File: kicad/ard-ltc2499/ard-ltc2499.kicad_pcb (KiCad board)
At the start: 2 copper layers, 53.3 x 68.6 mm, 55 parts, among them J1 Screw_Terminal_01x02, J2 Screw_Terminal_01x08, J3 Screw_Terminal_01x08, P1 Power, P2 Analog, P3 Digital, P4 Digital, P5 CONN_01X01, P6 CONN_01X01, P7 CONN_01X01, P8 CONN_01X01, Q1 BSS138, Q2 BSS138, SW1 SW_DIP_x08, SW2 JS202011SCQN, U1 LTC2499CUHF-PBF, U2 LT6654xxS6, U3 AP7381-50Y, U4 24AA025E64

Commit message: Adjusted text
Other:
- board text added: "+"
- board text added: "Arduino 5V"
- board text added: "Onboard 5V Reg"
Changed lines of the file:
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@@
   )
   (gr_line (start 150.749 116.586) (end 150.749 102.362) (layer "F.SilkS") (width 0.15))
+  (gr_line (start 134.0485 92.964) (end 137.9855 92.964) (layer "F.SilkS") (width 0.15))
   (gr_line (start 150.749 102.362) (end 154.051 102.362) (layer "F.SilkS") (width 0.15))
   (gr_poly
@@
   (gr_line (start 152.146 117.602) (end 152.146 121.666) (layer "F.SilkS") (width 0.15))
   (gr_line (start 150.749 116.586) (end 154.051 116.586) (layer "F.SilkS") (width 0.15))
+  (gr_line (start 128.9685 92.964) (end 132.9055 92.964) (layer "F.SilkS") (width 0.15))
   (gr_line (start 120.269 78.994) (end 114.427 78.994) (layer "Dwgs.User") (width 0.15))
   (gr_line (start 120.269 74.93) (end 120.269 78.994) (layer "Dwgs.User") (width 0.15))
@@
     (effects (font (size 0.889 0.7366) (thickness 0.1524)))
   )
+  (gr_text "Onboard\n5V Reg" (at 136.017 91.186) (layer "F.SilkS")
+    (effects (font (size 0.889 0.7366) (thickness 0.1524)))
+  )
   (gr_text "PWR" (at 137.16 119.38) (layer "F.SilkS")
     (effects (font (size 1.524 1.524) (thickness 0.3048)))
@@
     (effects (font (size 0.889 0.7366) (thickness 0.1524)))
   )
+  (gr_text "*" (at 161.671 75.692) (layer "F.SilkS")
+    (effects (font (size 1 1) (thickness 0.15)))
+  )
   (gr_text "0   1   2   3   4   5   6   7" (at 130.81 65.278 180) (layer "F.SilkS")
     (effects (font (size 1.016 0.7874) (thickness 0.1524)))
@@
     (effects (font (size 1.016 1.016) (thickness 0.1524)) (justify right))
   )
-  (gr_text "ARD-LTC2499 v2.0\nIowa Scaled Engineering\nhttp://www.iascaled.com\nCC BY-SA ©2024" (at 121.158 85.598) (layer "F.SilkS")
+  (gr_text "ARD-LTC2499 v2.0\nIowa Scaled Engineering\nhttp://www.iascaled.com\nCC BY-SA ©2024" (at 121.158 85.09) (layer "F.SilkS")
     (effects (font (size 1.016 1.016) (thickness 0.1524)) (justify left))
   )
@@
     (effects (font (size 0.7874 0.762) (thickness 0.1524)) (justify left))
   )
+  (gr_text "+" (at 131.191 121.031) (layer "F.SilkS")
+    (effects (font (size 1 1) (thickness 0.15)))
+  )
   (gr_text "CA2\nL   H" (at 152.4 104.394 90) (layer "F.SilkS")
     (effects (font (size 0.889 0.7366) (thickness 0.1524)))
@@
     (effects (font (size 1.016 0.7874) (thickness 0.1524)))
   )
+  (gr_text "Arduino\n5V" (at 130.937 91.186) (layer "F.SilkS")
+    (effects (font (size 0.889 0.7366) (thickness 0.1524)))
+  )
   (gr_text "10  11  12  13  14  15" (at 143.764 131.572) (layer "F.SilkS")
     (effects (font (size 1.016 0.7366) (thickness 0.1524)))
@@
     (effects (font (size 1.016 0.7874) (thickness 0.1524)) (justify left))
   )
-  (gr_text "*" (at 149.479 106.934) (layer "F.SilkS")
+  (gr_text "*" (at 149.479 107.061) (layer "F.SilkS")
     (effects (font (size 1 1) (thickness 0.15)))
   )

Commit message: Minor tweaks
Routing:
- net GND: track 112.0 -> 99.5 mm
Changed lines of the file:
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@@
     (property "Voltage" "16V")
     (attr smd)
-    (fp_text reference "C3" (at -0.254 -1.778) (layer "F.SilkS")
+    (fp_text reference "C3" (at 0 -1.778) (layer "F.SilkS")
       (effects (font (size 1 1) (thickness 0.15)))
     )
@@
   (segment (start 143.768 89.6226) (end 143.768 73.529) (width 0.25) (layer "F.Cu") (net 4))
   (segment (start 146.768 89.6226) (end 146.768 90.279) (width 0.254) (layer "F.Cu") (net 4))
-  (segment (start 166.116 123.317) (end 153.289 123.317) (width 0.381) (layer "F.Cu") (net 4))
   (segment (start 166.878 110.744) (end 167.005 110.871) (width 0.381) (layer "F.Cu") (net 4))
   (segment (start 133.5255 119.38) (end 133.5255 120.8555) (width 0.25) (layer "F.Cu") (net 4))
@@
   (segment (start 132.588 109.855) (end 132.588 108.331) (width 0.762) (layer "F.Cu") (net 4))
   (segment (start 146.768 94.5274) (end 148.6294 94.5274) (width 0.25) (layer "F.Cu") (net 4))
-  (segment (start 167.005 120.904) (end 167.005 122.428) (width 0.381) (layer "F.Cu") (net 4))
   (segment (start 147.470401 93.075001) (end 145.018001 93.075001) (width 0.25) (layer "F.Cu") (net 4))
   (segment (start 145.018001 93.075001) (end 144.018 92.075) (width 0.25) (layer "F.Cu") (net 4))
   (segment (start 144.517999 92.574999) (end 144.018 92.075) (width 0.25) (layer "F.Cu") (net 4))
-  (segment (start 167.005 122.428) (end 166.116 123.317) (width 0.381) (layer "F.Cu") (net 4))
   (segment (start 160.02 76.835) (end 160.02 75.311) (width 0.254) (layer "F.Cu") (net 4))
   (segment (start 167.005 110.871) (end 167.005 115.824) (width 0.381) (layer "F.Cu") (net 4))
@@
   (segment (start 167.005 115.824) (end 167.005 118.364) (width 0.381) (layer "F.Cu") (net 4))
   (segment (start 164.452 105.664) (end 166.37 105.664) (width 0.381) (layer "F.Cu") (net 4))
+  (segment (start 167.005 123.444) (end 167.005 120.904) (width 0.381) (layer "F.Cu") (net 4))
   (segment (start 166.37 105.664) (end 167.005 106.299) (width 0.381) (layer "F.Cu") (net 4))
   (segment (start 147.470401 92.574999) (end 148.708999 92.574999) (width 0.25) (layer "F.Cu") (net 4))
   (segment (start 162.179 76.962) (end 163.5155 76.962) (width 0.381) (layer "F.Cu") (net 4))
+  (segment (start 166.624 123.825) (end 167.005 123.444) (width 0.381) (layer "F.Cu") (net 4))
   (segment (start 145.268 89.6226) (end 145.268 90.825) (width 0.25) (layer "F.Cu") (net 4))
   (segment (start 147.470401 93.075001) (end 148.701001 93.075001) (width 0.25) (layer "F.Cu") (net 4))
@@
   (segment (start 144.82 72.477) (end 144.82 70.104) (width 0.25) (layer "F.Cu") (net 4))
   (segment (start 163.5155 76.962) (end 163.576 77.0225) (width 0.381) (layer "F.Cu") (net 4))
-  (via (at 153.289 123.317) (size 0.6) (drill 0.4) (layers "F.Cu" "B.Cu") (net 4))
+  (via (at 166.624 123.825) (size 0.6) (drill 0.4) (layers "F.Cu" "B.Cu") (net 4))
   (via (at 150.114 103.251) (size 0.6) (drill 0.4) (layers "F.Cu" "B.Cu") (free) (net 4))
   (via (at 160.02 75.311) (size 0.6) (drill 0.4) (layers "F.Cu" "B.Cu") (net 4))
@@
     (polygon
       (pts
-        (xy 153.796998 72.136)
-        (xy 164.465 72.136)
-        (xy 164.465 86.106)
-        (xy 153.796998 86.106)
-        (xy 153.796998 123.824376)
-        (xy 120.269 123.825)
+        (xy 167.386 72.136)
+        (xy 167.38601 124.713376)
+        (xy 120.269012 124.714)
         (xy 120.142 72.136)
-        (xy 153.796998 72.135376)
       )
     )

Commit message: Minor updates to text
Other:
- board text added: "A0 A1 L L"
- board text removed: "AD0 AD1"
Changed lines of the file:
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@@
     )
     (pad_to_mask_clearance 0)
-    (aux_axis_origin 110.998 126.365)
+    (aux_axis_origin 119.634 132.715)
     (pcbplotparams
       (layerselection 0x0000030_80000001)
@@
   )
   (gr_line (start 150.749 116.586) (end 150.749 102.362) (layer "F.SilkS") (width 0.15))
+  (gr_line (start 150.749 117.348) (end 154.051 117.348) (layer "F.SilkS") (width 0.15))
   (gr_line (start 134.0485 92.964) (end 137.9855 92.964) (layer "F.SilkS") (width 0.15))
   (gr_line (start 150.749 102.362) (end 154.051 102.362) (layer "F.SilkS") (width 0.15))
@@
       (xy 148.107136 78.517728)
     ) (layer "F.SilkS") (width 0) (fill solid))
+  (gr_line (start 150.749 121.92) (end 154.051 121.92) (layer "F.SilkS") (width 0.15))
   (gr_poly
     (pts
@@
       (xy 144.291095 76.196139)
     ) (layer "F.SilkS") (width 0) (fill solid))
-  (gr_line (start 152.146 117.602) (end 152.146 121.666) (layer "F.SilkS") (width 0.15))
+  (gr_line (start 150.749 117.348) (end 150.749 121.92) (layer "F.SilkS") (width 0.15))
   (gr_line (start 150.749 116.586) (end 154.051 116.586) (layer "F.SilkS") (width 0.15))
   (gr_line (start 128.9685 92.964) (end 132.9055 92.964) (layer "F.SilkS") (width 0.15))
@@
   (gr_line (start 172.974 128.651) (end 172.974 64.135) (layer "Edge.Cuts") (width 0.15))
   (gr_line (start 160.02 130.175) (end 171.45 130.175) (layer "Edge.Cuts") (width 0.15))
-  (gr_text "EEP ADR" (at 151.257 119.634 90) (layer "F.SilkS")
+  (gr_text "EEP ADR" (at 149.86 119.634 90) (layer "F.SilkS")
     (effects (font (size 0.889 0.7366) (thickness 0.1524)))
   )
@@
     (effects (font (size 0.7874 0.762) (thickness 0.1524)) (justify left))
   )
-  (gr_text "LTC2499 ADR" (at 149.987 116.713 90) (layer "F.SilkS")
+  (gr_text "LTC2499 ADR" (at 149.86 116.713 90) (layer "F.SilkS")
     (effects (font (size 0.889 0.7366) (thickness 0.1524)) (justify left))
   )
@@
     (effects (font (size 0.889 0.7366) (thickness 0.1524)))
   )
-  (gr_text "\nAD0 AD1" (at 152.4 119.634 90) (layer "F.SilkS")
+  (gr_text "A0  A1\nL   L" (at 152.4 119.634 90) (layer "F.SilkS")
     (effects (font (size 0.889 0.7366) (thickness 0.1524)))
   )
@@
     (effects (font (size 1.016 0.7366) (thickness 0.1524)))
   )
-  (gr_text "4.096V REF   COM" (at 154.686 65.278 180) (layer "F.SilkS")
+  (gr_text "4.096V REF  COM" (at 154.178 65.278 180) (layer "F.SilkS")
     (effects (font (size 1.016 0.7874) (thickness 0.1524)) (justify left))
   )

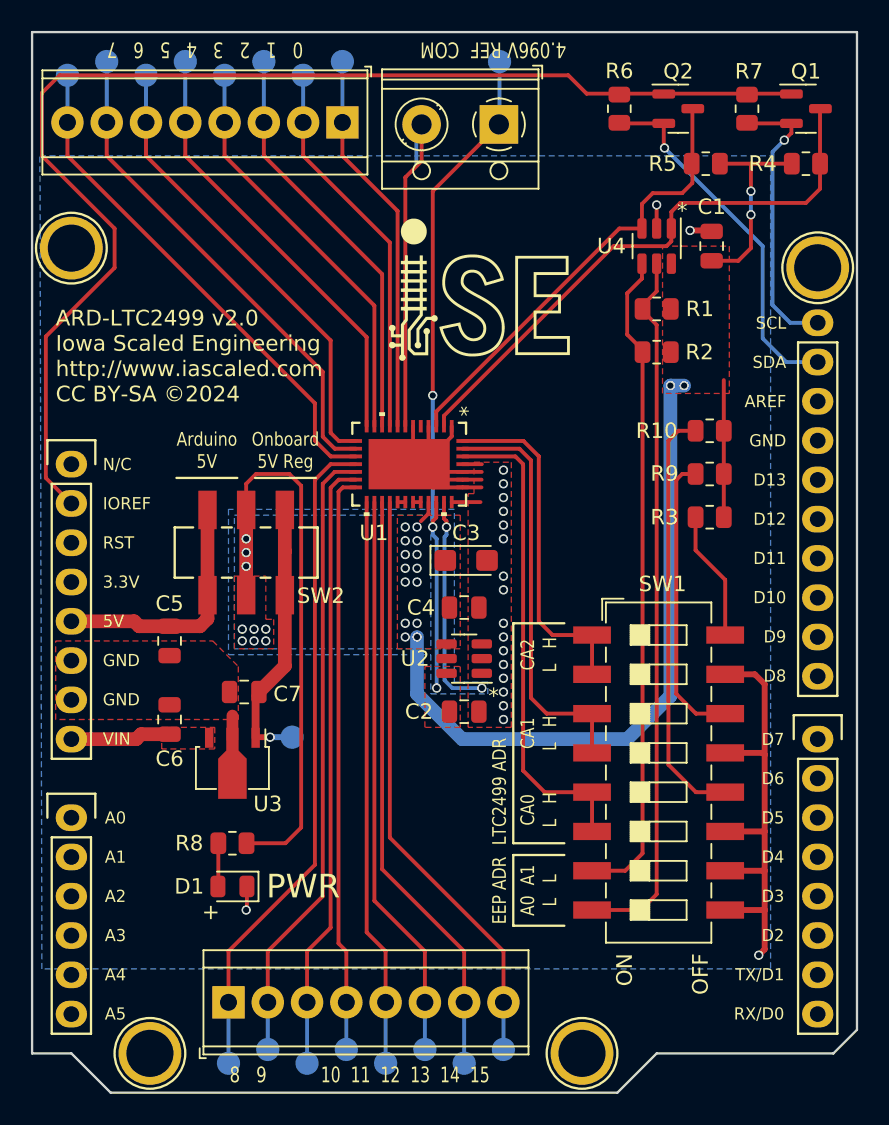
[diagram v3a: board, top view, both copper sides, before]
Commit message: Minor adjustments to metal traces
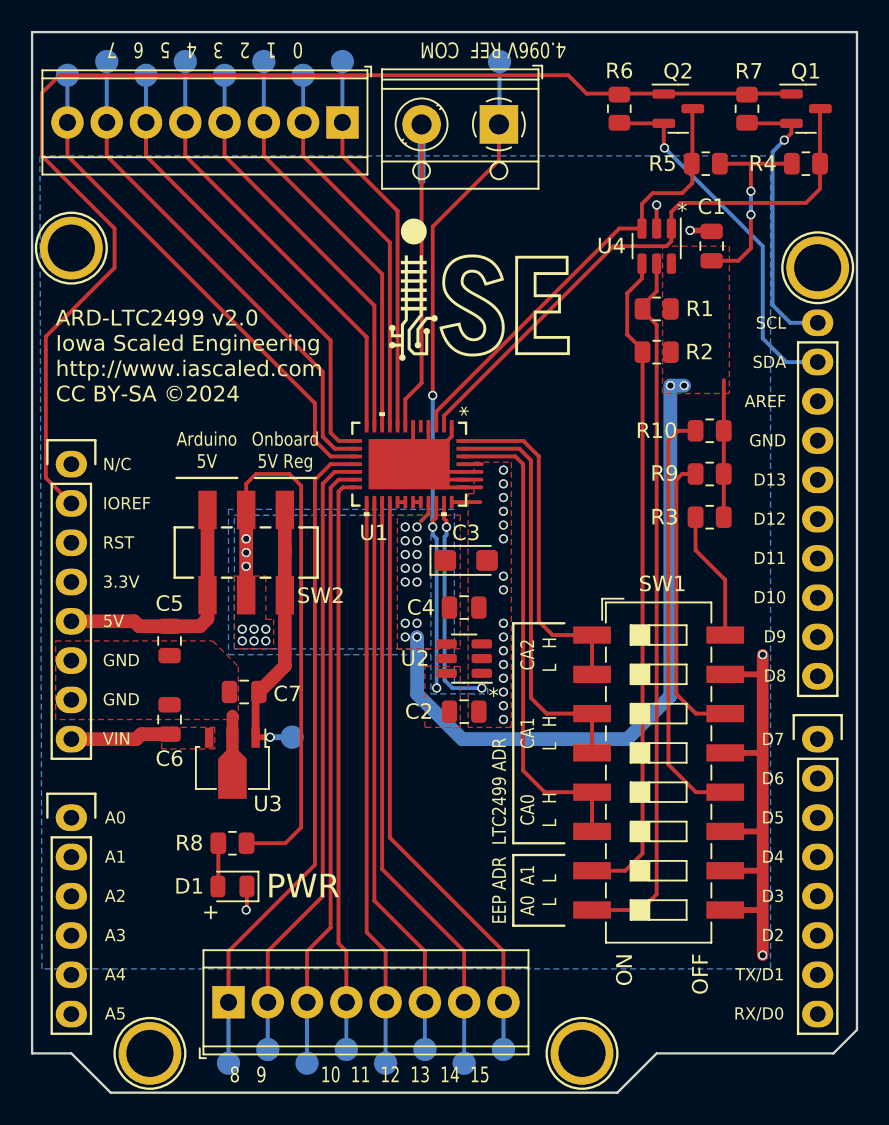
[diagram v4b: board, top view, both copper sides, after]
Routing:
- net GND: track 99.5 -> 102.1 mm, vias 22 -> 23
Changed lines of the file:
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@@
   (segment (start 130.977 95.0341) (end 130.977 100.5459) (width 0.889) (layer "F.Cu") (net 3))
   (segment (start 128.524 102.555) (end 130.49 102.555) (width 0.889) (layer "F.Cu") (net 3))
-  (segment (start 143.768 73.529) (end 144.82 72.477) (width 0.25) (layer "F.Cu") (net 4))
   (segment (start 164.452 110.744) (end 166.878 110.744) (width 0.381) (layer "F.Cu") (net 4))
   (segment (start 146.268001 94.5274) (end 146.268001 95.595001) (width 0.25) (layer "F.Cu") (net 4))
-  (segment (start 167.005 118.364) (end 167.005 120.904) (width 0.381) (layer "F.Cu") (net 4))
+  (segment (start 166.878 123.825) (end 166.878 104.394) (width 0.762) (layer "F.Cu") (net 4))
   (segment (start 144.972 92.075) (end 144.018 92.075) (width 0.254) (layer "F.Cu") (net 4))
-  (segment (start 143.768 89.6226) (end 143.768 73.529) (width 0.25) (layer "F.Cu") (net 4))
   (segment (start 146.768 89.6226) (end 146.768 90.279) (width 0.254) (layer "F.Cu") (net 4))
   (segment (start 166.878 110.744) (end 167.005 110.871) (width 0.381) (layer "F.Cu") (net 4))
@@
   (segment (start 147.470401 92.075) (end 148.717 92.075) (width 0.25) (layer "F.Cu") (net 4))
   (segment (start 164.452 118.364) (end 167.005 118.364) (width 0.381) (layer "F.Cu") (net 4))
+  (segment (start 143.768 89.6226) (end 143.768 87.88) (width 0.254) (layer "F.Cu") (net 4))
   (segment (start 145.518 93.575) (end 144.018 92.075) (width 0.25) (layer "F.Cu") (net 4))
   (segment (start 132.588 109.855) (end 132.588 108.331) (width 0.762) (layer "F.Cu") (net 4))
@@
   (segment (start 144.517999 92.574999) (end 144.018 92.075) (width 0.25) (layer "F.Cu") (net 4))
   (segment (start 160.02 76.835) (end 160.02 75.311) (width 0.254) (layer "F.Cu") (net 4))
-  (segment (start 167.005 110.871) (end 167.005 115.824) (width 0.381) (layer "F.Cu") (net 4))
   (segment (start 164.452 120.904) (end 167.005 120.904) (width 0.381) (layer "F.Cu") (net 4))
   (segment (start 146.768 90.279) (end 144.972 92.075) (width 0.254) (layer "F.Cu") (net 4))
@@
   (segment (start 147.470401 92.574999) (end 144.517999 92.574999) (width 0.25) (layer "F.Cu") (net 4))
   (segment (start 146.431 95.758) (end 146.431 96.139) (width 0.25) (layer "F.Cu") (net 4))
-  (segment (start 167.005 106.299) (end 167.005 110.871) (width 0.381) (layer "F.Cu") (net 4))
+  (segment (start 164.452 105.664) (end 167.005 105.664) (width 0.381) (layer "F.Cu") (net 4))
   (segment (start 147.470401 93.575) (end 145.518 93.575) (width 0.25) (layer "F.Cu") (net 4))
-  (segment (start 167.005 115.824) (end 167.005 118.364) (width 0.381) (layer "F.Cu") (net 4))
-  (segment (start 164.452 105.664) (end 166.37 105.664) (width 0.381) (layer "F.Cu") (net 4))
-  (segment (start 167.005 123.444) (end 167.005 120.904) (width 0.381) (layer "F.Cu") (net 4))
-  (segment (start 166.37 105.664) (end 167.005 106.299) (width 0.381) (layer "F.Cu") (net 4))
   (segment (start 147.470401 92.574999) (end 148.708999 92.574999) (width 0.25) (layer "F.Cu") (net 4))
   (segment (start 162.179 76.962) (end 163.5155 76.962) (width 0.381) (layer "F.Cu") (net 4))
-  (segment (start 166.624 123.825) (end 167.005 123.444) (width 0.381) (layer "F.Cu") (net 4))
+  (segment (start 143.768 87.88) (end 144.819995 86.828005) (width 0.254) (layer "F.Cu") (net 4))
   (segment (start 145.268 89.6226) (end 145.268 90.825) (width 0.25) (layer "F.Cu") (net 4))
   (segment (start 147.470401 93.075001) (end 148.701001 93.075001) (width 0.25) (layer "F.Cu") (net 4))
+  (segment (start 144.819995 86.828005) (end 144.819995 70.104) (width 0.254) (layer "F.Cu") (net 4))
   (segment (start 144.268 89.6226) (end 144.268 91.825) (width 0.25) (layer "F.Cu") (net 4))
-  (segment (start 144.82 72.477) (end 144.82 70.104) (width 0.25) (layer "F.Cu") (net 4))
   (segment (start 163.5155 76.962) (end 163.576 77.0225) (width 0.381) (layer "F.Cu") (net 4))
-  (via (at 166.624 123.825) (size 0.6) (drill 0.4) (layers "F.Cu" "B.Cu") (net 4))
+  (via (at 166.878 123.825) (size 0.6) (drill 0.4) (layers "F.Cu" "B.Cu") (net 4))
   (via (at 150.114 103.251) (size 0.6) (drill 0.4) (layers "F.Cu" "B.Cu") (free) (net 4))
   (via (at 160.02 75.311) (size 0.6) (drill 0.4) (layers "F.Cu" "B.Cu") (net 4))
@@
   (via (at 150.114 102.362) (size 0.6) (drill 0.4) (layers "F.Cu" "B.Cu") (free) (net 4))
   (via (at 150.114 92.456) (size 0.6) (drill 0.4) (layers "F.Cu" "B.Cu") (free) (net 4))
+  (via (at 166.878 104.394) (size 0.6) (drill 0.4) (layers "F.Cu" "B.Cu") (net 4))
   (via (at 150.114 106.807) (size 0.6) (drill 0.4) (layers "F.Cu" "B.Cu") (free) (net 4))
   (via (at 150.114 107.696) (size 0.6) (drill 0.4) (layers "F.Cu" "B.Cu") (free) (net 4))
@@
   (via (at 150.114 95.123) (size 0.6) (drill 0.4) (layers "F.Cu" "B.Cu") (free) (net 4))
   (via (at 133.477 120.904) (size 0.6) (drill 0.4) (layers "F.Cu" "B.Cu") (net 4))
-  (segment (start 144.479 70.104) (end 144.479 72.644) (width 0.25) (layer "B.Cu") (net 4))
+  (segment (start 144.819995 70.104) (end 144.819995 73.747005) (width 0.508) (layer "B.Cu") (net 4))
   (segment (start 146.431 96.647) (end 146.304 96.774) (width 0.25) (layer "B.Cu") (net 4))
   (segment (start 146.304 106.045) (end 146.812 106.553) (width 0.25) (layer "B.Cu") (net 4))
@@
   (segment (start 144.526 106.934) (end 147.447 109.855) (width 0.889) (layer "B.Cu") (net 11))
   (segment (start 147.447 109.855) (end 158.115 109.855) (width 0.889) (layer "B.Cu") (net 11))
+  (segment (start 149.82 72.43) (end 149.82 70.104) (width 0.25) (layer "F.Cu") (net 12))
   (segment (start 145.767999 95.532001) (end 145.542 95.758) (width 0.25) (layer "F.Cu") (net 12))
   (segment (start 145.542 95.758) (end 145.542 96.139) (width 0.25) (layer "F.Cu") (net 12))
-  (segment (start 145.542 87.63) (end 145.542 74.422) (width 0.25) (layer "F.Cu") (net 12))
-  (segment (start 145.542 74.422) (end 149.82 70.144) (width 0.25) (layer "F.Cu") (net 12))
+  (segment (start 145.542 87.63) (end 145.542 76.708) (width 0.25) (layer "F.Cu") (net 12))
   (segment (start 145.767999 94.5274) (end 145.767999 95.532001) (width 0.25) (layer "F.Cu") (net 12))
-  (segment (start 149.82 70.144) (end 149.82 70.104) (width 0.25) (layer "F.Cu") (net 12))
+  (segment (start 145.542 76.708) (end 149.82 72.43) (width 0.25) (layer "F.Cu") (net 12))
   (via (at 145.796 106.553) (size 0.6) (drill 0.4) (layers "F.Cu" "B.Cu") (net 12))
   (via (at 145.542 96.139) (size 0.6) (drill 0.4) (layers "F.Cu" "B.Cu") (net 12))
